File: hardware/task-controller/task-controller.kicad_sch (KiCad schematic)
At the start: 48 parts, among them J1 USB_C_Receptacle_USB2.0_16P, SW50 BOOTSEL, SW51 RST, SW52 User, U1 XC6206PxxxMR, U3 W25Q32JVSS, U4 RP2040, U5 FM24C64B, Y1 12MHz

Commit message: most of rest of schematic
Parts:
- added J6: Conn_01x06, Connector_PinHeader_2.54mm:PinHeader_1x06_P2.54mm_Vertical, symbol Connector_Generic:Conn_01x06
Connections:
- net BUTTON: now also U4.41 (GPIO29_ADC3); no longer U4.37 (GPIO25)
- net Button Matrix/C4: now also U4.32 (GPIO21); no longer U4.29 (GPIO18)
- net Button Matrix/C5: now also U4.34 (GPIO22); no longer U4.30 (GPIO19)
- net Button Matrix/C6: now also U4.35 (GPIO23); no longer U4.31 (GPIO20)
- net Button Matrix/C7: now also U4.36 (GPIO24); no longer U4.32 (GPIO21)
- net EEPROM_WP: no longer U4.6 (GPIO4)
- net GND: now also R22.1, J6.6 (Pin_6)
- net UART_RX: now also J6.2 (Pin_2)
- net UART_TX: now also J6.3 (Pin_3)
- net VDD: no longer R22.1
- net at R10.1: now also U4.6 (GPIO4)
- net RTC_INT: now reaches U4.40 (GPIO28_ADC2)
- new net CTS_(NC): J6.5 (Pin_5)
- new net RTX_(NC): J6.1 (Pin_1)
- new net SD_CS: U4.37 (GPIO25)
- new net SPI_MISO: U4.31 (GPIO20)
- new net SPI_MOSI: U4.30 (GPIO19)
- new net SPI_SCK: U4.29 (GPIO18)
- new net VCC_(NC): J6.4 (Pin_4)
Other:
- added sheet Peripherals (peripherals.kicad_sch)
- moved on the sheet: D1, R10, R22

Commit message: started layout
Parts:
- removed D2: SK6812, LED_SMD:LED_SK6812_PLCC4_5.0x5.0mm_P3.2mm, symbol LED:SK6812
- removed R13: 1k, Resistor_SMD:R_0402_1005Metric, symbol Device:R
- removed R17: 500R, Resistor_SMD:R_0603_1608Metric, symbol Device:R
- removed SW52: User, cat:TS-1088-AR02016, symbol Switch:SW_Push
- C10, C11, C12, C13, C14, C15, C16, C17, C18, C19, C21, C7: footprint Capacitor_SMD:C_0603_1608Metric -> Capacitor_SMD:C_0402_1005Metric; LCSC Part # C14663 -> C1525
- R12: footprint Connector_JST:JST_XH_B2B-XH-AM_1x02_P2.50mm_Vertical -> Connector_JST:JST_PH_B2B-PH-K_1x02_P2.00mm_Vertical
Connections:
- net VDD is gone; now on net +3V3: C13.2, C14.2, C15.2, C16.2, C17.2, C18.2, C19.2, C20.2, C21.1, C7.2, R11.1, R20.2, R21.2, R3.1, R9.2, U3.8 (VCC), U4.1 (IOVDD), U4.10 (IOVDD), U4.22 (IOVDD), U4.33 (IOVDD), U4.42 (IOVDD), U4.43 (ADC_AVDD), U4.44 (VREG_IN), U4.48 (USB_VDD), U4.49 (IOVDD), U5.8 (VDD)
- no-connect marks 5 -> 4
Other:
- sheet User Interface ports: added BUTTON; removed none
- note removed: "May not be needed"
- note removed: "Short resistor footprint so it can be populated and the trace cut if it turns out to be needed"
- moved on the sheet: C1, C8, U1

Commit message: stuff
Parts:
- removed C19: 0.1uF, Capacitor_SMD:C_0402_1005Metric, symbol Device:C
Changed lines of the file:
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@@
-		)
-	)
-	(symbol
-		(lib_id "Device:C")
-		(at 195.58 25.4 180)
-		(unit 1)
-		(exclude_from_sim no)
-		(in_bom yes)
-		(on_board yes)
-		(dnp no)
-		(fields_autoplaced yes)
-		(property "Reference" "C19"
-			(at 199.39 24.1299 0)
-			(effects
-				(font
-					(size 1.27 1.27)
-				)
-				(justify right)
-			)
-		)
-		(property "Value" "0.1uF"
-			(at 199.39 26.6699 0)
-			(effects
-				(font
-					(size 1.27 1.27)
-				)
-				(justify right)
-			)
-		)
-		(property "Footprint" "Capacitor_SMD:C_0402_1005Metric"
-			(at 194.6148 21.59 0)
-			(effects
-				(font
-					(size 1.27 1.27)
-				)
-				(hide yes)
-			)
-		)
-		(property "Datasheet" "~"
-			(at 195.58 25.4 0)
-			(effects
-				(font
-					(size 1.27 1.27)
-				)
-				(hide yes)
-			)
-		)
-		(property "Description" "Unpolarized capacitor"
-			(at 195.58 25.4 0)
-			(effects
-				(font
-					(size 1.27 1.27)
-				)
-				(hide yes)
-			)
-		)
-		(property "Cost" ""
-			(at 195.58 25.4 0)
-			(effects
-				(font
-					(size 1.27 1.27)
-				)
-				(hide yes)
-			)
-		)
-		(property "LCSC Part #" "C1525 "
-			(at 195.58 25.4 0)
-			(effects
-				(font
-					(size 1.27 1.27)
-				)
-				(hide yes)
-			)
-		)
-		(property "DK #" ""
-			(at 195.58 25.4 0)
-			(effects
-				(font
-					(size 1.27 1.27)
-				)
-				(hide yes)
-			)
-		)
-		(property "JLCPCB Rotation Offset" ""
-			(at 195.58 25.4 0)
-			(effects
-				(font
-					(size 1.27 1.27)
-				)
-				(hide yes)
-			)
-		)
-		(pin "2"
-		)
-		(pin "1"
-		)
-		(instances
-			(project "reminder-sequin"
-				(path "/3313c311-f70a-45a8-bbf4-c9e4cbd18d5c"
-					(reference "C19")
-					(unit 1)
-				)
-			)
 		)
 	)

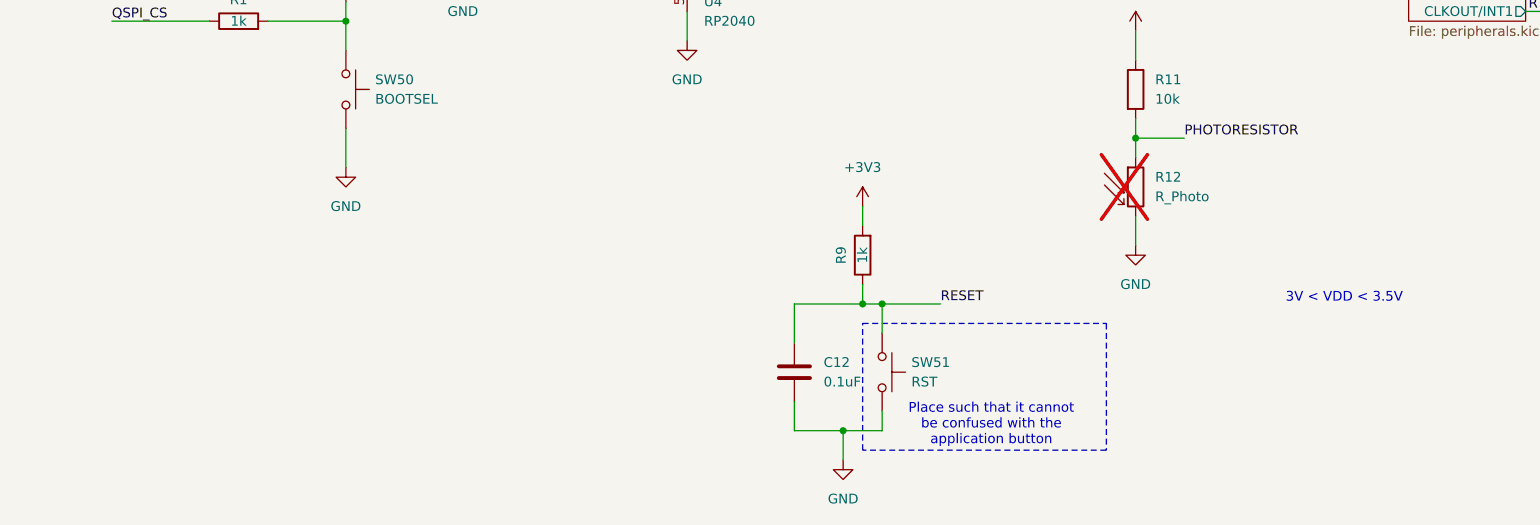
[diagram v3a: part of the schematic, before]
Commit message: changed board size
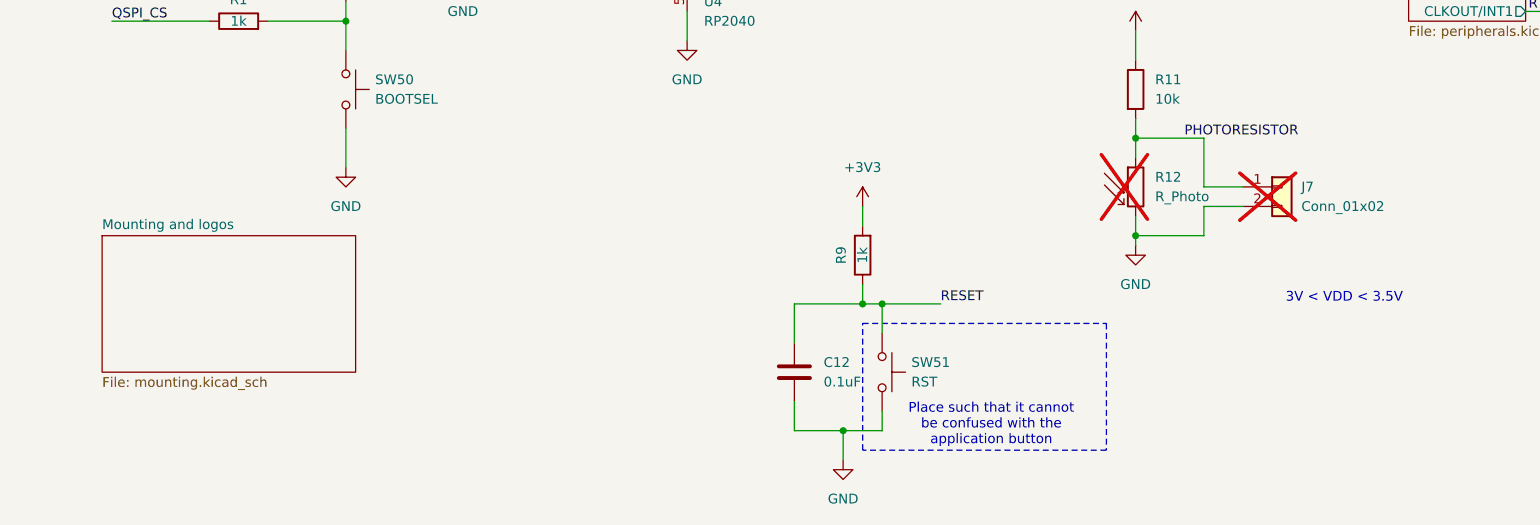
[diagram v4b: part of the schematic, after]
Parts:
- added J7: Conn_01x02, Connector_PinHeader_2.54mm:PinHeader_1x02_P2.54mm_Vertical, symbol Connector_Generic:Conn_01x02
- R12: footprint Connector_JST:JST_PH_B2B-PH-K_1x02_P2.00mm_Vertical -> Connector_JST:JST_PH_B2B-PH-SM4-TB_1x02-1MP_P2.00mm_Vertical; LCSC Part # (none) -> C64658
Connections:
- net GND: now also J7.2 (Pin_2)
- net PHOTORESISTOR: now also J7.1 (Pin_1)
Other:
- added sheet Mounting and logos (mounting.kicad_sch)
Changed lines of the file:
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@@
 	)
 	(junction
+		(at 160.02 160.02)
+		(diameter 0)
+		(color 0 0 0 0)
+	)
+	(junction
 		(at 229.87 101.6)
 		(diameter 0)
@@
 	(wire
 		(pts
+			(xy 168.91 153.67) (xy 168.91 147.32)
+		)
+		(stroke
+			(width 0)
+			(type default)
+		)
+	)
+	(wire
+		(pts
 			(xy 45.72 105.41) (xy 45.72 109.22)
 		)
@@
 	(wire
 		(pts
+			(xy 160.02 160.02) (xy 160.02 161.29)
+		)
+		(stroke
+			(width 0)
+			(type default)
+		)
+	)
+	(wire
+		(pts
 			(xy 111.76 25.4) (xy 111.76 39.37)
 		)
@@
 	(wire
 		(pts
+			(xy 168.91 156.21) (xy 168.91 160.02)
+		)
+		(stroke
+			(width 0)
+			(type default)
+		)
+	)
+	(wire
+		(pts
 			(xy 38.1 55.88) (xy 52.07 55.88)
 		)
@@
 	(wire
 		(pts
+			(xy 168.91 160.02) (xy 160.02 160.02)
+		)
+		(stroke
+			(width 0)
+			(type default)
+		)
+	)
+	(wire
+		(pts
 			(xy 234.95 88.9) (xy 238.76 88.9)
 		)
@@
 	(wire
 		(pts
+			(xy 173.99 153.67) (xy 168.91 153.67)
+		)
+		(stroke
+			(width 0)
+			(type default)
+		)
+	)
+	(wire
+		(pts
 			(xy 109.22 25.4) (xy 109.22 39.37)
 		)
@@
 	(wire
 		(pts
-			(xy 160.02 157.48) (xy 160.02 161.29)
+			(xy 160.02 157.48) (xy 160.02 160.02)
 		)
 		(stroke
@@
 	(wire
 		(pts
-			(xy 160.02 147.32) (xy 166.37 147.32)
+			(xy 160.02 147.32) (xy 168.91 147.32)
 		)
 		(stroke
@@
 	(wire
 		(pts
+			(xy 173.99 156.21) (xy 168.91 156.21)
+		)
+		(stroke
+			(width 0)
+			(type default)
+		)
+	)
+	(wire
+		(pts
 			(xy 143.51 107.95) (xy 127 107.95)
 		)
@@
 	)
 	(symbol
+		(lib_id "Connector_Generic:Conn_01x02")
+		(at 179.07 153.67 0)
+		(unit 1)
+		(exclude_from_sim no)
+		(in_bom no)
+		(on_board yes)
+		(dnp yes)
+		(fields_autoplaced yes)
+		(property "Reference" "J7"
+			(at 181.61 153.6699 0)
+			(effects
+				(font
+					(size 1.27 1.27)
+				)
+				(justify left)
+			)
+		)
+		(property "Value" "Conn_01x02"
+			(at 181.61 156.2099 0)
+			(effects
+				(font
+					(size 1.27 1.27)
+				)
+				(justify left)
+			)
+		)
+		(property "Footprint" "Connector_PinHeader_2.54mm:PinHeader_1x02_P2.54mm_Vertical"
+			(at 179.07 153.67 0)
+			(effects
+				(font
+					(size 1.27 1.27)
+				)
+				(hide yes)
+			)
+		)
+		(property "Datasheet" "~"
+			(at 179.07 153.67 0)
+			(effects
+				(font
+					(size 1.27 1.27)
+				)
+				(hide yes)
+			)
+		)
+		(property "Description" "Generic connector, single row, 01x02, script generated (kicad-library-utils/schlib/autogen/connector/)"
+			(at 179.07 153.67 0)
+			(effects
+				(font
+					(size 1.27 1.27)
+				)
+				(hide yes)
+			)
+		)
+		(pin "1"
+		)
+		(pin "2"
+		)
+		(instances
+			(project ""
+				(path "/3313c311-f70a-45a8-bbf4-c9e4cbd18d5c"
+					(reference "J7")
+					(unit 1)
+				)
+			)
+		)
+	)
+	(symbol
 		(lib_id "Device:C")
 		(at 138.43 25.4 180)
@@
 			)
 		)
-		(property "Footprint" "Connector_JST:JST_PH_B2B-PH-K_1x02_P2.00mm_Vertical"
+		(property "Footprint" "Connector_JST:JST_PH_B2B-PH-SM4-TB_1x02-1MP_P2.00mm_Vertical"
 			(at 161.29 160.02 90)
 			(effects
@@
 			)
 		)
+		(property "LCSC Part #" "C64658"
+			(at 160.02 153.67 0)
+			(effects
+				(font
+					(size 1.27 1.27)
+				)
+				(hide yes)
+			)
+		)
 		(pin "2"
 		)
@@
 				)
 			)
+		)
+	)
+	(sheet
+		(at 25.4 160.02)
+		(size 33.02 17.78)
+		(fields_autoplaced yes)
+		(stroke
+			(width 0.1524)
+			(type solid)
+		)
+		(fill
+			(color 0 0 0 0.0000)
+		)
+		(property "Sheetname" "Mounting and logos"
+			(at 25.4 159.3084 0)
+			(effects
+				(font
+					(size 1.27 1.27)
+				)
+				(justify left bottom)
+			)
+		)
+		(property "Sheetfile" "mounting.kicad_sch"
+			(at 25.4 178.3846 0)
+			(effects
+				(font
+					(size 1.27 1.27)
+				)
+				(justify left top)
+			)
+		)
+		(instances
+			(project "task-controller"
+				(path "/3313c311-f70a-45a8-bbf4-c9e4cbd18d5c"
+					(page "5")
+				)
+			)

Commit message: electrical design passes DRC
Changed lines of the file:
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@@
-		)
-	)
-	(label "SD_CS"
-		(at 26.67 93.98 0)
-		(effects
-			(font
-				(size 1.27 1.27)
-			)
-			(justify left bottom)
 		)
 	)

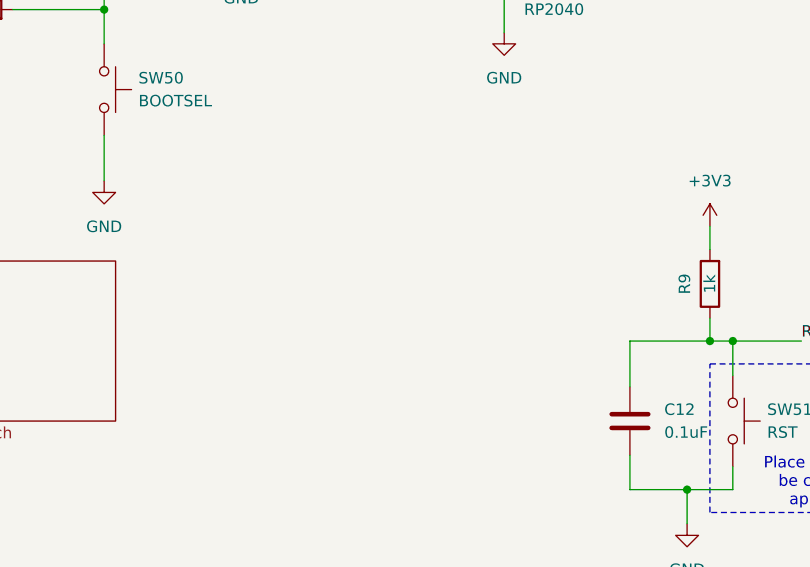
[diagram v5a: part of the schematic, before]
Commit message: added graphics
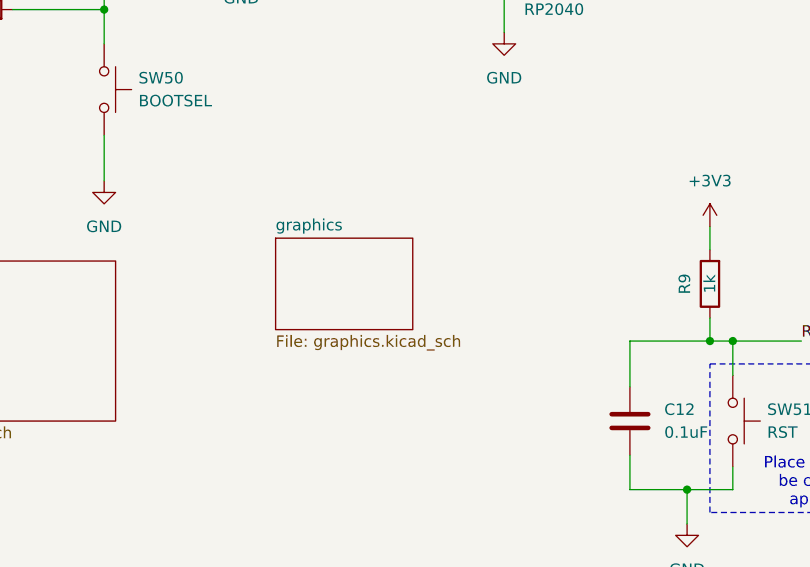
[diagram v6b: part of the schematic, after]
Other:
- added sheet graphics (graphics.kicad_sch)
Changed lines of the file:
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@@
+	)
+	(sheet
+		(at 76.2 157.48)
+		(size 15.24 10.16)
+		(fields_autoplaced yes)
+		(stroke
+			(width 0.1524)
+			(type solid)
+		)
+		(fill
+			(color 0 0 0 0.0000)
+		)
+		(property "Sheetname" "graphics"
+			(at 76.2 156.7684 0)
+			(effects
+				(font
+					(size 1.27 1.27)
+				)
+				(justify left bottom)
+			)
+		)
+		(property "Sheetfile" "graphics.kicad_sch"
+			(at 76.2 168.2246 0)
+			(effects
+				(font
+					(size 1.27 1.27)
+				)
+				(justify left top)
+			)
+		)
+		(instances
+			(project "task-controller"
+				(path "/3313c311-f70a-45a8-bbf4-c9e4cbd18d5c"
+					(page "6")
+				)
+			)
+		)
 	)
 	(sheet

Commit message: whatever updates
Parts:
- added J8: SWD, Connector_PinHeader_2.54mm:PinHeader_1x06_P2.54mm_Vertical, symbol Connector_Generic:Conn_01x06
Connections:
- net +3V3: now also J8.2 (Pin_2)
- net GND: now also J8.6 (Pin_6)
- net RESET: now also J8.1 (Pin_1)
- net SWCLK: now reaches U4.24 (SWCLK)
- net SWCLK: now also J8.4 (Pin_4)
- net SWDIO: now reaches U4.25 (SWD)
- net SWDIO: now also J8.3 (Pin_3)
- no-connect marks 4 -> 3

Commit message: preparing for production export
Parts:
- added J9: I2C, Connector_JST:JST_PH_B4B-PH-K_1x04_P2.00mm_Vertical, symbol Connector_Generic:Conn_01x04
- U5: LCSC Part # (none) -> C914923
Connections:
- net +3V3: now also J9.2 (Pin_2)
- net GND: now also J9.1 (Pin_1)
- net SCL: now also J9.4 (Pin_4)
- net SDA: now also J9.3 (Pin_3)
